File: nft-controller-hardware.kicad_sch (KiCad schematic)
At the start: 28 parts, among them J0 Micro_SD_Card_Det, J1 Conn_01x03_Male, J2 Conn_01x03_Male, J3 Conn_01x03_Male, J4 Conn_01x03_Male, U0 DS3231M, U1 ADS1115IDGS

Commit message: Size all SMD resistors to 2012.
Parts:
- R0, R1, R10, R11, R2, R3, R4, R5, R6, R7, R8, R9: footprint (none) -> Resistor_SMD:R_0805_2012Metric
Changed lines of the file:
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@@
     (property "Reference" "R0" (id 0) (at 31.75 76.2 90))
     (property "Value" "4.7kΩ" (id 1) (at 31.75 78.74 90))
-    (property "Footprint" "" (id 2) (at 31.75 81.28 0)
+    (property "Footprint" "Resistor_SMD:R_0805_2012Metric" (id 2) (at 31.75 81.28 0)
       (effects (font (size 1.27 1.27)) hide)
     )
@@
     (property "Reference" "R5" (id 0) (at 114.3 74.93 90))
     (property "Value" "4.7kΩ" (id 1) (at 114.3 72.39 90))
-    (property "Footprint" "" (id 2) (at 114.3 69.85 0)
+    (property "Footprint" "Resistor_SMD:R_0805_2012Metric" (id 2) (at 114.3 69.85 0)
       (effects (font (size 1.27 1.27)) hide)
     )
@@
     (property "Reference" "R7" (id 0) (at 114.3 92.71 90))
     (property "Value" "4.7kΩ" (id 1) (at 114.3 90.17 90))
-    (property "Footprint" "" (id 2) (at 114.3 87.63 0)
+    (property "Footprint" "Resistor_SMD:R_0805_2012Metric" (id 2) (at 114.3 87.63 0)
       (effects (font (size 1.27 1.27)) hide)
     )
@@
     (property "Reference" "R1" (id 0) (at 34.29 93.98 90))
     (property "Value" "4.7kΩ" (id 1) (at 34.29 91.44 90))
-    (property "Footprint" "" (id 2) (at 34.29 88.9 0)
+    (property "Footprint" "Resistor_SMD:R_0805_2012Metric" (id 2) (at 34.29 88.9 0)
       (effects (font (size 1.27 1.27)) hide)
     )
@@
     (property "Reference" "R11" (id 0) (at 179.07 149.86 90))
     (property "Value" "4.7kΩ" (id 1) (at 179.07 147.32 90))
-    (property "Footprint" "" (id 2) (at 179.07 144.78 0)
+    (property "Footprint" "Resistor_SMD:R_0805_2012Metric" (id 2) (at 179.07 144.78 0)
       (effects (font (size 1.27 1.27)) hide)
     )
@@
     (property "Reference" "R8" (id 0) (at 62.23 129.54 90))
     (property "Value" "4.7kΩ" (id 1) (at 62.23 132.08 90))
-    (property "Footprint" "" (id 2) (at 62.23 134.62 0)
+    (property "Footprint" "Resistor_SMD:R_0805_2012Metric" (id 2) (at 62.23 134.62 0)
       (effects (font (size 1.27 1.27)) hide)
     )
@@
     (property "Reference" "R10" (id 0) (at 173.99 127 90))
     (property "Value" "4.7kΩ" (id 1) (at 173.99 129.54 90))
-    (property "Footprint" "" (id 2) (at 173.99 132.08 0)
+    (property "Footprint" "Resistor_SMD:R_0805_2012Metric" (id 2) (at 173.99 132.08 0)
       (effects (font (size 1.27 1.27)) hide)
     )
@@
     (property "Reference" "R9" (id 0) (at 62.23 149.86 90))
     (property "Value" "4.7kΩ" (id 1) (at 62.23 147.32 90))
-    (property "Footprint" "" (id 2) (at 62.23 144.78 0)
+    (property "Footprint" "Resistor_SMD:R_0805_2012Metric" (id 2) (at 62.23 144.78 0)
       (effects (font (size 1.27 1.27)) hide)
     )
@@
     (property "Reference" "R3" (id 0) (at 114.3 34.29 90))
     (property "Value" "4.7kΩ" (id 1) (at 114.3 31.75 90))
-    (property "Footprint" "" (id 2) (at 114.3 29.21 0)
+    (property "Footprint" "Resistor_SMD:R_0805_2012Metric" (id 2) (at 114.3 29.21 0)
       (effects (font (size 1.27 1.27)) hide)
     )
@@
     (property "Reference" "R6" (id 0) (at 114.3 83.82 90))
     (property "Value" "4.7kΩ" (id 1) (at 114.3 81.28 90))
-    (property "Footprint" "" (id 2) (at 114.3 78.74 0)
+    (property "Footprint" "Resistor_SMD:R_0805_2012Metric" (id 2) (at 114.3 78.74 0)
       (effects (font (size 1.27 1.27)) hide)
     )
@@
     (property "Reference" "R2" (id 0) (at 114.3 25.4 90))
     (property "Value" "4.7kΩ" (id 1) (at 114.3 22.86 90))
-    (property "Footprint" "" (id 2) (at 114.3 20.32 0)
+    (property "Footprint" "Resistor_SMD:R_0805_2012Metric" (id 2) (at 114.3 20.32 0)
       (effects (font (size 1.27 1.27)) hide)
     )
@@
     (property "Reference" "R4" (id 0) (at 114.3 43.18 90))
     (property "Value" "4.7kΩ" (id 1) (at 114.3 40.64 90))
-    (property "Footprint" "" (id 2) (at 114.3 38.1 0)
+    (property "Footprint" "Resistor_SMD:R_0805_2012Metric" (id 2) (at 114.3 38.1 0)
       (effects (font (size 1.27 1.27)) hide)
     )
@@
     )
     (path "/0b172d1f-339f-4591-b391-d2a4ed4d42c3"
-      (reference "R0") (unit 1) (value "4.7kΩ") (footprint "")
+      (reference "R0") (unit 1) (value "4.7kΩ") (footprint "Resistor_SMD:R_0805_2012Metric")
     )
     (path "/59faf929-8296-4635-b12d-2800ce62b201"
-      (reference "R1") (unit 1) (value "4.7kΩ") (footprint "")
+      (reference "R1") (unit 1) (value "4.7kΩ") (footprint "Resistor_SMD:R_0805_2012Metric")
     )
     (path "/bb1de491-4b94-4f94-8df8-d95d59ba46ae"
-      (reference "R2") (unit 1) (value "4.7kΩ") (footprint "")
+      (reference "R2") (unit 1) (value "4.7kΩ") (footprint "Resistor_SMD:R_0805_2012Metric")
     )
     (path "/b19a3df7-28ef-49ae-a0c7-ada0b4971916"
-      (reference "R3") (unit 1) (value "4.7kΩ") (footprint "")
+      (reference "R3") (unit 1) (value "4.7kΩ") (footprint "Resistor_SMD:R_0805_2012Metric")
     )
     (path "/db3ee492-4f46-40e4-874d-e053e011be5d"
-      (reference "R4") (unit 1) (value "4.7kΩ") (footprint "")
+      (reference "R4") (unit 1) (value "4.7kΩ") (footprint "Resistor_SMD:R_0805_2012Metric")
     )
     (path "/0bbc0beb-1100-4671-b546-a8e3c0b9d7bd"
-      (reference "R5") (unit 1) (value "4.7kΩ") (footprint "")
+      (reference "R5") (unit 1) (value "4.7kΩ") (footprint "Resistor_SMD:R_0805_2012Metric")
     )
     (path "/b6d61560-a56b-483a-a3c4-9222570cbaa5"
-      (reference "R6") (unit 1) (value "4.7kΩ") (footprint "")
+      (reference "R6") (unit 1) (value "4.7kΩ") (footprint "Resistor_SMD:R_0805_2012Metric")
     )
     (path "/313ce9ee-e0cc-47bb-9201-5e5e91bfc052"
-      (reference "R7") (unit 1) (value "4.7kΩ") (footprint "")
+      (reference "R7") (unit 1) (value "4.7kΩ") (footprint "Resistor_SMD:R_0805_2012Metric")
     )
     (path "/80138220-4276-495f-ae14-7fdf06bfec0c"
-      (reference "R8") (unit 1) (value "4.7kΩ") (footprint "")
+      (reference "R8") (unit 1) (value "4.7kΩ") (footprint "Resistor_SMD:R_0805_2012Metric")
     )
     (path "/94bb0b95-88c4-4e75-8f6a-7e4ebac94ec6"
-      (reference "R9") (unit 1) (value "4.7kΩ") (footprint "")
+      (reference "R9") (unit 1) (value "4.7kΩ") (footprint "Resistor_SMD:R_0805_2012Metric")
     )
     (path "/86214f25-5bc5-4736-b61e-abcad4e76c1d"
-      (reference "R10") (unit 1) (value "4.7kΩ") (footprint "")
+      (reference "R10") (unit 1) (value "4.7kΩ") (footprint "Resistor_SMD:R_0805_2012Metric")
     )
     (path "/7044d50a-f6ed-439e-ad8c-78b47efca99a"
-      (reference "R11") (unit 1) (value "4.7kΩ") (footprint "")
+      (reference "R11") (unit 1) (value "4.7kΩ") (footprint "Resistor_SMD:R_0805_2012Metric")
     )
     (path "/ab55a345-fabe-4cbb-9366-8ee841f1136b"

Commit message: Update footprints & datasheets.
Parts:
- BT0: footprint (none) -> Battery:BatteryHolder_Keystone_3000_1x12mm
- J0: footprint (none) -> Connector_Card:microSD_HC_Hirose_DM3AT-SF-PEJM5

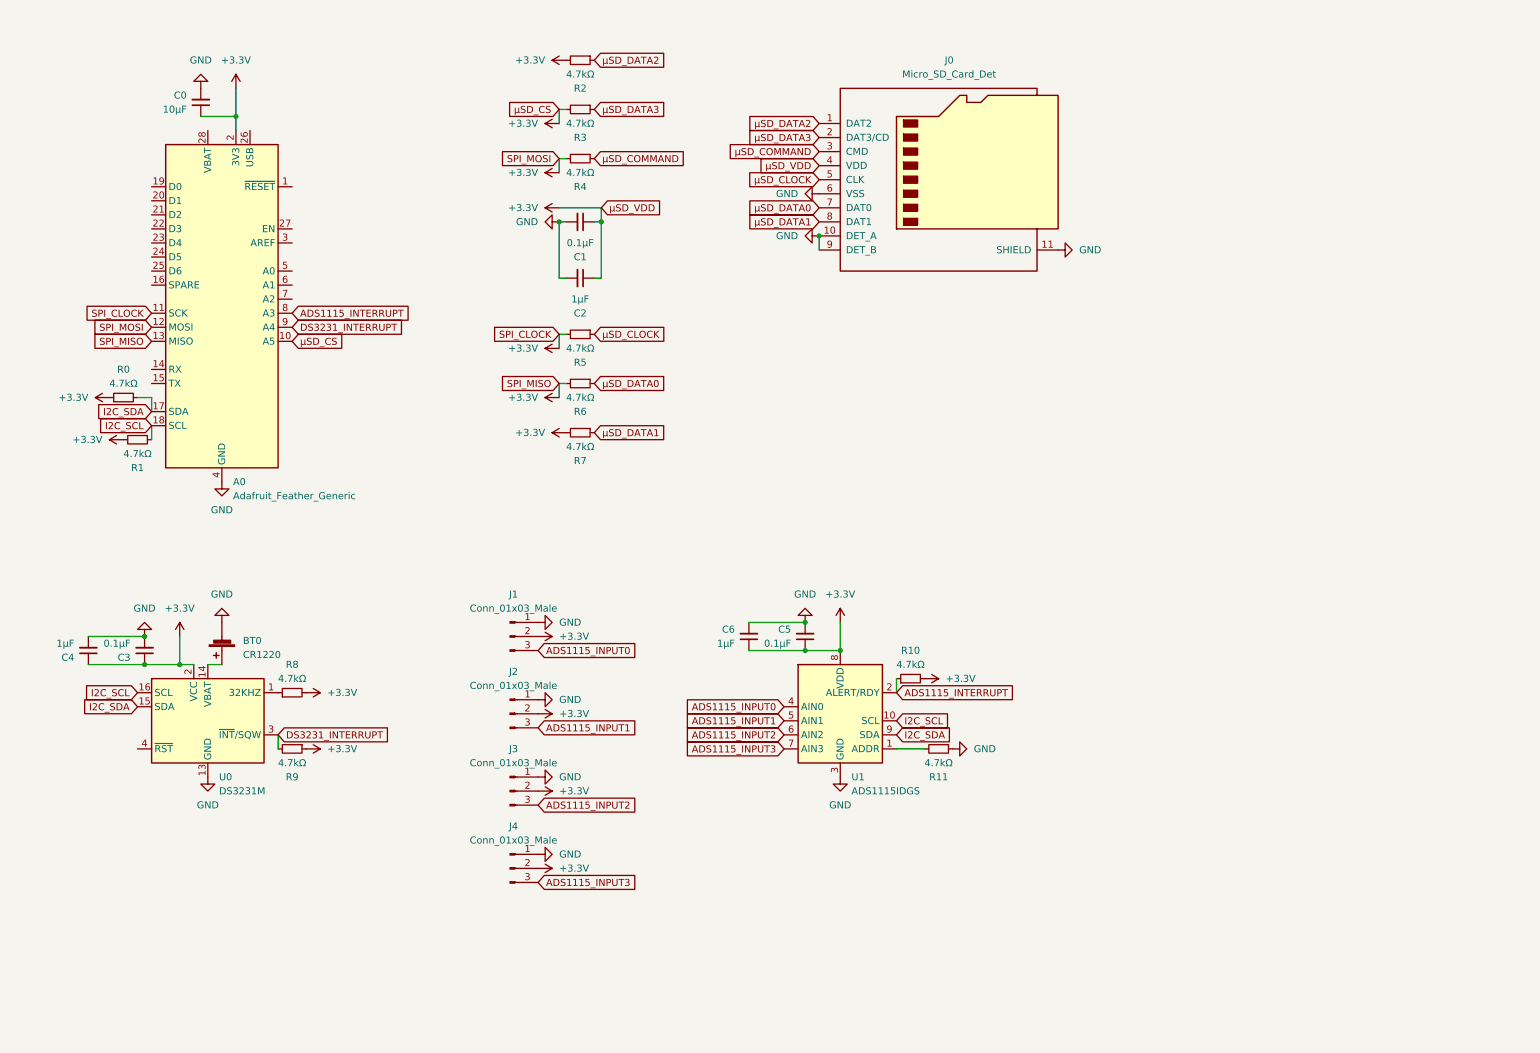
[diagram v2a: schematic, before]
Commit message: Redesign the memory/RTC/ADC expansion board.
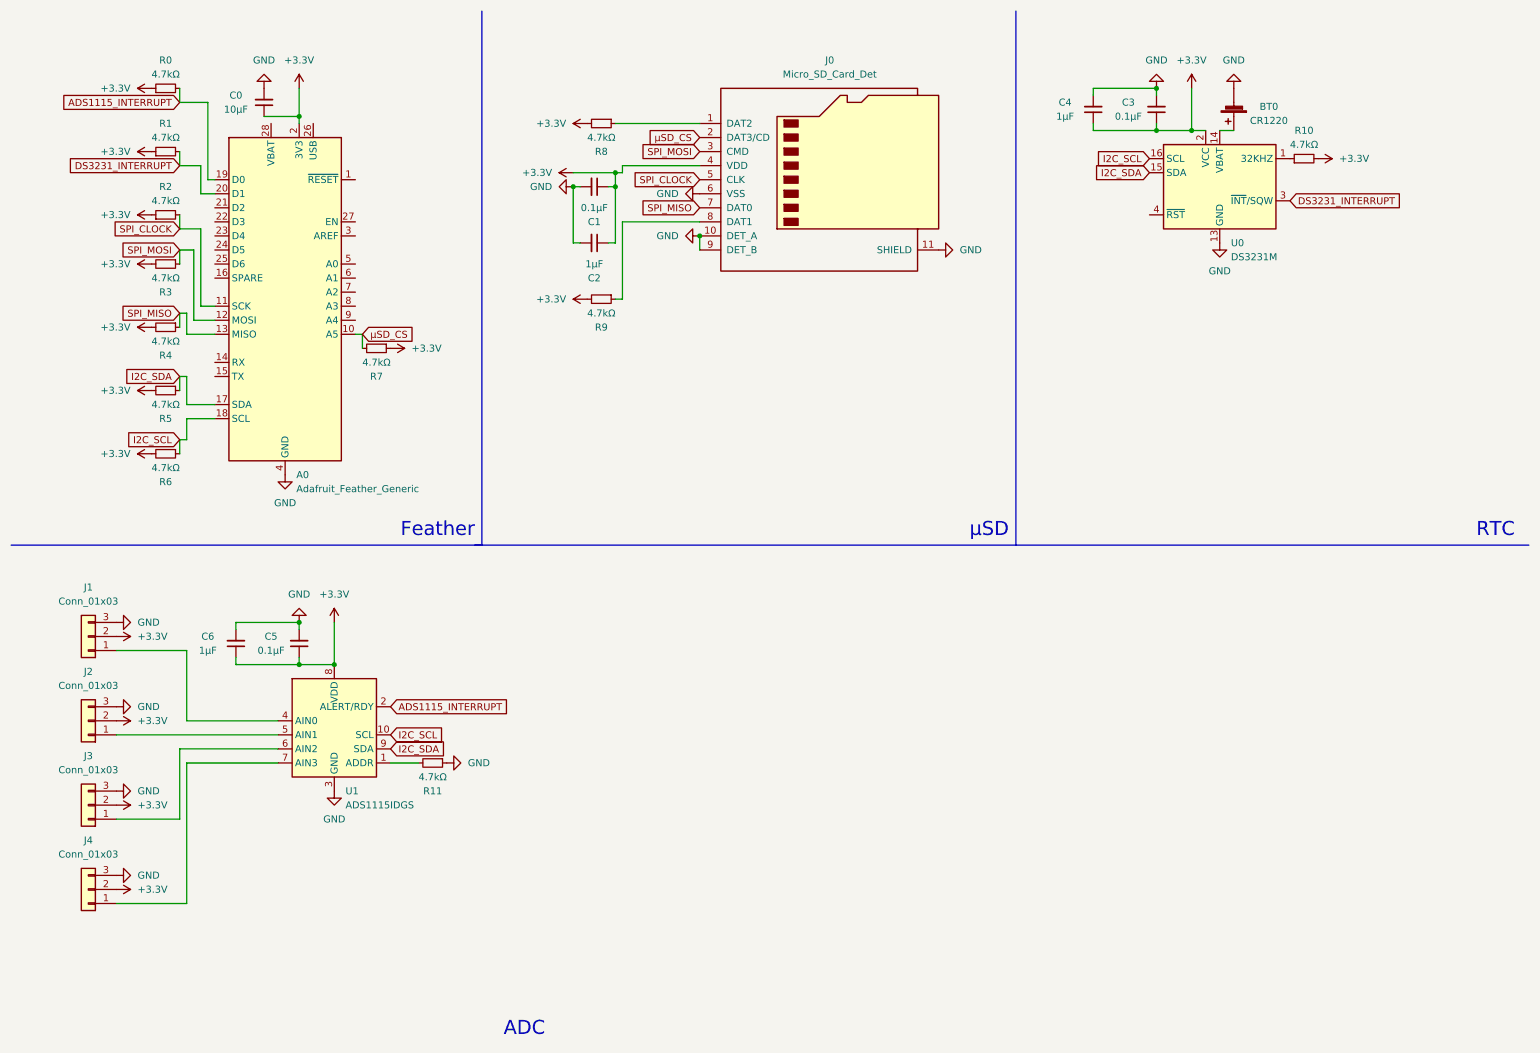
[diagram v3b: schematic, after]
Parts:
- removed J1, J2, J3, J4: Conn_01x03_Male, Connector_JST:JST_SH_SM03B-SRSS-TB_1x03-1MP_P1.00mm_Horizontal, symbol Connector:Conn_01x03_Male
- removed R10, R6: 4.7kΩ, Resistor_SMD:R_0805_2012Metric, symbol Device:R_Small
- added J1, J2, J3, J4: Conn_01x03, Connector_JST:JST_SH_SM03B-SRSS-TB_1x03-1MP_P1.00mm_Horizontal, symbol Connector_Generic:Conn_01x03
- added R1, R2: 4.7kΩ, Resistor_SMD:R_0402_1005Metric, symbol Device:R_Small
- C0, C1, C2, C3, C4, C5, C6: footprint Capacitor_SMD:C_0805_2012Metric -> Capacitor_SMD:C_0402_1005Metric
- R0, R11, R3, R4, R5, R7, R9: footprint Resistor_SMD:R_0805_2012Metric -> Resistor_SMD:R_0402_1005Metric
- R10: renamed from R8; footprint Resistor_SMD:R_0805_2012Metric -> Resistor_SMD:R_0402_1005Metric
- R6: renamed from R1; footprint Resistor_SMD:R_0805_2012Metric -> Resistor_SMD:R_0402_1005Metric
- R8: renamed from R2; footprint Resistor_SMD:R_0805_2012Metric -> Resistor_SMD:R_0402_1005Metric
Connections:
- net μSD_DATA0 is gone; now on net SPI_MISO: J0.7 (DAT0)
- net +3V3: now also R7.1, R9.2, J1.2 (Pin_2), J2.2 (Pin_2), J3.2 (Pin_2), J4.2 (Pin_2), R1.1, R2.1; no longer A0.10 (A5), A0.11 (SCK), A0.12 (MOSI), A0.13 (MISO), R7.2, R9.1
- net ADS1115_INTERRUPT: now also A0.19 (D0), R0.2; no longer A0.8 (A3)
- net DS3231_INTERRUPT: now also A0.20 (D1), R1.2; no longer A0.9 (A4), R9.2
- net GND: now also J1.3 (Pin_3), J2.3 (Pin_3), J3.3 (Pin_3), J4.3 (Pin_3)
- net I2C_SDA: now also R5.1; no longer R0.2
- net ADS1115_INPUT0: no longer names the net of U1.4 (AIN0)
- net ADS1115_INPUT0: now also J1.1 (Pin_1)
- net ADS1115_INPUT1: no longer names the net of U1.5 (AIN1)
- net ADS1115_INPUT1: now also J2.1 (Pin_1)
- net ADS1115_INPUT2: no longer names the net of U1.6 (AIN2)
- net ADS1115_INPUT2: now also J3.1 (Pin_1)
- net ADS1115_INPUT3: no longer names the net of U1.7 (AIN3)
- net ADS1115_INPUT3: now also J4.1 (Pin_1)
- net μSD_CLOCK renamed SPI_CLOCK
- net SPI_CLOCK: now also A0.11 (SCK), R2.2; no longer R5.1
- net μSD_COMMAND renamed SPI_MISO
- net SPI_MISO: now also A0.13 (MISO); no longer J0.3 (CMD)
- net μSD_DATA1: no longer names the net of J0.8 (DAT1)
- net μSD_DATA1: now also R9.1; no longer R7.1
- net μSD_DATA2: no longer names the net of J0.1 (DAT2), R8.1
- net μSD_DATA3 renamed SPI_MOSI
- net SPI_MOSI: now also A0.12 (MOSI), J0.3 (CMD); no longer J0.2 (DAT3/CD)
- new net μSD_CS: A0.10 (A5), J0.2 (DAT3/CD), R7.2
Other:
- note added: "ADC"
- note added: "Feather"
- note added: "RTC"
- note added: "μSD"
- moved on the sheet: A0, BT0, C0, C1, C2, J0, R10, R11, R6, R8, U0, U1
